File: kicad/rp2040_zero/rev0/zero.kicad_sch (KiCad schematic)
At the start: 13 parts, among them J1 jtag, J2 Conn_01x03_Socket, J5 Debug port, U1 RP2040-Zero, U3 3V->VTREF, U4 VTREF->3V, U5 VTREF<->3V, U6 RT9013-33GB

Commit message: RP2040: Carrier board
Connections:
- net SWIO_DIR is gone; now on net SWIO_DIR_3V: U1.21 (GP11)
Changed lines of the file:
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@@
 		)
 	)
-	(global_label "SWIO_DIR"
+	(global_label "SWIO_DIR_3V"
 		(shape output)
 		(at 55.88 63.5 270)
@@
 		)
 		(property "Intersheetrefs" "${INTERSHEET_REFS}"
-			(at 55.88 75.1938 90)
+			(at 55.88 78.4595 90)
 			(effects
 				(font

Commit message: cleanup
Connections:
- net INOUT_NRESET: now also U1.7 (GP26)
- net OUT_SWDCLK_3V: now also U1.20 (GP12); no longer U1.19 (GP13)
- net OUT_SWDIO_3V: now also U1.19 (GP13); no longer U1.20 (GP12)
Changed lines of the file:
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@@
+	(wire
+		(pts
+			(xy 34.29 45.72) (xy 40.64 45.72)
+		)
+		(stroke
+			(width 0)
+			(type default)
+		)
+	)
 	(wire
 		(pts
@@
 			(width 0)
 			(type default)
+		)
+	)
+	(global_label "INOUT_NRESET"
+		(shape input)
+		(at 34.29 45.72 180)
+		(fields_autoplaced yes)
+		(effects
+			(font
+				(size 1.27 1.27)
+			)
+			(justify right)
+		)
+		(property "Intersheetrefs" "${INTERSHEET_REFS}"
+			(at 17.6977 45.72 0)
+			(effects
+				(font
+					(size 1.27 1.27)
+				)
+				(justify right)
+				(hide yes)
+			)
 		)
 	)
@@
 	(global_label "OUT_SWDCLK_3V"
 		(shape output)
-		(at 50.8 63.5 270)
-		(fields_autoplaced yes)
-		(effects
-			(font
-				(size 1.27 1.27)
-			)
-			(justify right)
-		)
-		(property "Intersheetrefs" "${INTERSHEET_REFS}"
-			(at 50.8 81.8461 90)
+		(at 53.34 63.5 270)
+		(fields_autoplaced yes)
+		(effects
+			(font
+				(size 1.27 1.27)
+			)
+			(justify right)
+		)
+		(property "Intersheetrefs" "${INTERSHEET_REFS}"
+			(at 53.34 81.8461 90)
 			(effects
 				(font
@@
 	(global_label "OUT_SWDIO_3V"
 		(shape bidirectional)
-		(at 53.34 63.5 270)
-		(fields_autoplaced yes)
-		(effects
-			(font
-				(size 1.27 1.27)
-			)
-			(justify right)
-		)
-		(property "Intersheetrefs" "${INTERSHEET_REFS}"
-			(at 53.34 81.3246 90)
-			(effects
-				(font
+		(at 50.8 63.5 270)
+		(fields_autoplaced yes)
+		(effects
+			(font
+				(size 1.27 1.27)
+			)
+			(justify right)
+		)
+		(property "Intersheetrefs" "${INTERSHEET_REFS}"
+			(at 50.8 81.3246 90)
+			(effects
+				(font

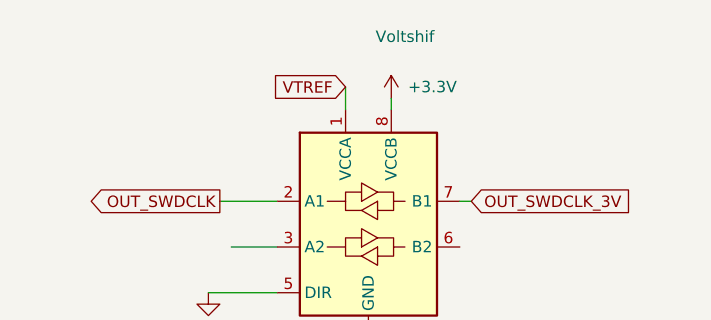
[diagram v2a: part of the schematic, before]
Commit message: kicad: update to correct voltage translator footprint
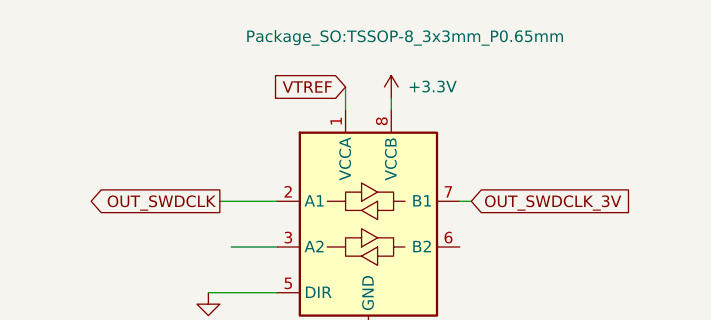
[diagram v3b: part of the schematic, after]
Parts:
- U3: footprint Voltshif -> Package_SO:TSSOP-8_3x3mm_P0.65mm
- U4, U5: footprint Package_SO:VSSOP-8_2.3x2mm_P0.5mm -> Package_SO:TSSOP-8_3x3mm_P0.65mm
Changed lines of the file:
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@@
 			)
 		)
-		(property "Footprint" "Package_SO:VSSOP-8_2.3x2mm_P0.5mm"
+		(property "Footprint" "Package_SO:TSSOP-8_3x3mm_P0.65mm"
 			(at 114.3 97.79 0)
 			(effects
@@
 			)
 		)
-		(property "Footprint" "Voltshif"
+		(property "Footprint" "Package_SO:TSSOP-8_3x3mm_P0.65mm"
 			(at 118.364 23.622 0)
 			(effects
@@
 			)
 		)
-		(property "Footprint" "Package_SO:VSSOP-8_2.3x2mm_P0.5mm"
+		(property "Footprint" "Package_SO:TSSOP-8_3x3mm_P0.65mm"
 			(at 113.03 137.16 0)
 			(effects

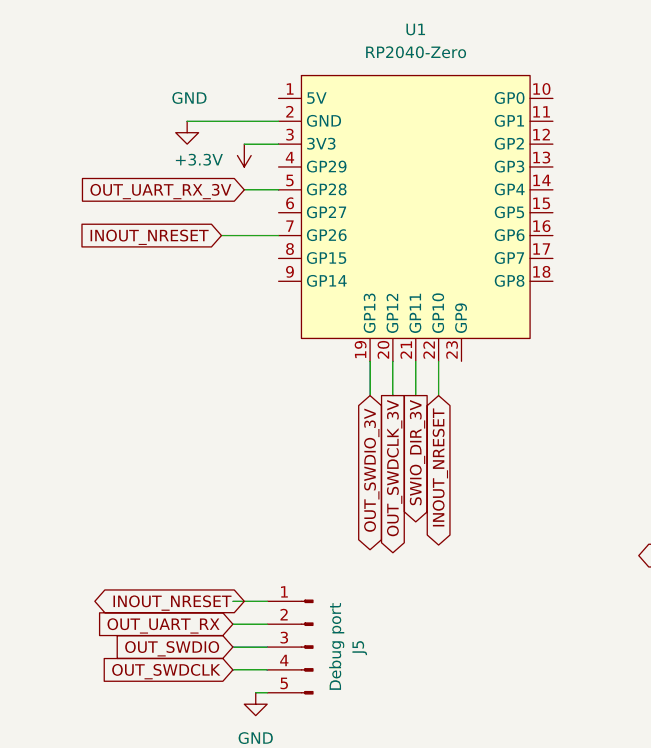
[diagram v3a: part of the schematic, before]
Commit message: kicad : map the uart RX to GPIO9 on the carrier
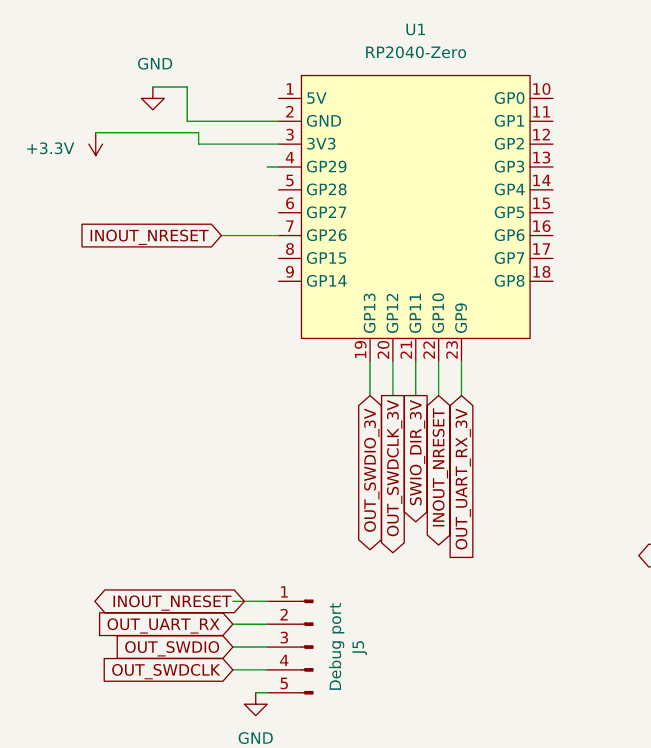
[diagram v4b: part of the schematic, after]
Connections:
- net OUT_UART_RX_3V: now also U1.23 (GP9); no longer U1.5 (GP28)
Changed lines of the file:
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@@
 	(wire
 		(pts
+			(xy 60.96 59.69) (xy 60.96 63.5)
+		)
+		(stroke
+			(width 0)
+			(type default)
+		)
+	)
+	(wire
+		(pts
+			(xy 31.75 35.56) (xy 40.64 35.56)
+		)
+		(stroke
+			(width 0)
+			(type default)
+		)
+	)
+	(wire
+		(pts
 			(xy 41.91 119.38) (xy 44.45 119.38)
 		)
@@
 	(wire
 		(pts
+			(xy 30.48 29.21) (xy 26.67 29.21)
+		)
+		(stroke
+			(width 0)
+			(type default)
+		)
+	)
+	(wire
+		(pts
 			(xy 123.19 81.28) (xy 127 81.28)
 		)
@@
 	(wire
 		(pts
-			(xy 36.83 35.56) (xy 40.64 35.56)
+			(xy 20.32 34.29) (xy 31.75 34.29)
 		)
 		(stroke
@@
 	(wire
 		(pts
+			(xy 39.37 38.1) (xy 40.64 38.1)
+		)
+		(stroke
+			(width 0)
+			(type default)
+		)
+	)
+	(wire
+		(pts
 			(xy 41.91 121.92) (xy 44.45 121.92)
 		)
@@
 	(wire
 		(pts
+			(xy 30.48 33.02) (xy 30.48 29.21)
+		)
+		(stroke
+			(width 0)
+			(type default)
+		)
+	)
+	(wire
+		(pts
 			(xy 82.55 156.21) (xy 82.55 158.75)
 		)
@@
 	(wire
 		(pts
-			(xy 142.24 102.87) (xy 147.32 102.87)
+			(xy 31.75 34.29) (xy 31.75 35.56)
 		)
 		(stroke
@@
 	(wire
 		(pts
-			(xy 58.42 163.83) (xy 72.39 163.83)
+			(xy 142.24 102.87) (xy 147.32 102.87)
 		)
 		(stroke
@@
 	(wire
 		(pts
-			(xy 100.33 91.44) (xy 102.87 91.44)
+			(xy 58.42 163.83) (xy 72.39 163.83)
 		)
 		(stroke
@@
 	(wire
 		(pts
-			(xy 115.57 68.58) (xy 115.57 71.12)
+			(xy 100.33 91.44) (xy 102.87 91.44)
 		)
 		(stroke
@@
 	(wire
 		(pts
-			(xy 58.42 59.69) (xy 58.42 63.5)
+			(xy 115.57 68.58) (xy 115.57 71.12)
 		)
 		(stroke
@@
 	(wire
 		(pts
-			(xy 36.83 40.64) (xy 40.64 40.64)
+			(xy 58.42 59.69) (xy 58.42 63.5)
 		)
 		(stroke
@@
 	(global_label "OUT_UART_RX_3V"
 		(shape input)
-		(at 36.83 40.64 180)
+		(at 60.96 63.5 270)
 		(fields_autoplaced yes)
 		(effects
@@
 		)
 		(property "Intersheetrefs" "${INTERSHEET_REFS}"
-			(at 17.8791 40.64 0)
+			(at 60.96 82.4509 90)
 			(effects
 				(font
@@
 	(symbol
 		(lib_id "power:+3.3V")
-		(at 36.83 35.56 180)
+		(at 20.32 34.29 180)
 		(unit 1)
 		(exclude_from_sim no)
@@
 		(dnp no)
 		(property "Reference" "#PWR01"
-			(at 36.83 31.75 0)
+			(at 20.32 30.48 0)
 			(effects
 				(font
@@
 		)
 		(property "Value" "+3.3V"
-			(at 31.75 37.338 0)
+			(at 15.24 36.068 0)
 			(effects
 				(font
@@
 		)
 		(property "Footprint" ""
-			(at 36.83 35.56 0)
+			(at 20.32 34.29 0)
 			(effects
 				(font
@@
 		)
 		(property "Datasheet" ""
-			(at 36.83 35.56 0)
+			(at 20.32 34.29 0)
 			(effects
 				(font
@@
 		)
 		(property "Description" ""
-			(at 36.83 35.56 0)
+			(at 20.32 34.29 0)
 			(effects
 				(font
@@
 	(symbol
 		(lib_id "power:GND")
-		(at 30.48 33.02 0)
+		(at 26.67 29.21 0)
 		(unit 1)
 		(exclude_from_sim no)
@@
 		(dnp no)
 		(property "Reference" "#PWR02"
-			(at 30.48 39.37 0)
+			(at 26.67 35.56 0)
 			(effects
 				(font
@@
 		)
 		(property "Value" "GND"
-			(at 30.734 30.48 0)
+			(at 26.924 26.67 0)
 			(effects
 				(font
@@
 		)
 		(property "Footprint" ""
-			(at 30.48 33.02 0)
+			(at 26.67 29.21 0)
 			(effects
 				(font
@@
 		)
 		(property "Datasheet" ""
-			(at 30.48 33.02 0)
+			(at 26.67 29.21 0)
 			(effects
 				(font
@@
 		)
 		(property "Description" ""
-			(at 30.48 33.02 0)
+			(at 26.67 29.21 0)
 			(effects
 				(font
